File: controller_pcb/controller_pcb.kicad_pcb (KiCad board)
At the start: 2 copper layers, 64.5 x 51.5 mm, 0 parts

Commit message: PCB layout editing
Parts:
- added C1: CL21B106KOQNNNE, Controller_Footprints:CAPC2012X140N, F.Cu at (185.0, 107.5)
- added C2: CL21B106KOQNNNE, Controller_Footprints:CAPC2012X140N, F.Cu at (185.0, 110.3)
- added C3: CL21B106KOQNNNE, Controller_Footprints:CAPC2012X140N, F.Cu at (185.0, 113.1)
- added C4: CL21B106KOQNNNE, Controller_Footprints:CAPC2012X140N, F.Cu at (185.0, 115.9)
- added C5: CL21B106KOQNNNE, Controller_Footprints:CAPC2012X140N, F.Cu at (185.0, 118.7)
- added IC1: ATTINY85V-10SU, Controller_Footprints:SOIC127P798X216-8N, F.Cu at (181.8, 132.1)
- added R1: ERJP06F1002V, Controller_Footprints:ERJP06D1000V, F.Cu at (109.7, 107.0)
- added R2: ERJP06F1002V, Controller_Footprints:ERJP06D1000V, F.Cu at (109.7, 114.0)
- added R3: ERJP06F1002V, Controller_Footprints:ERJP06D1000V, F.Cu at (154.7, 106.5)
- added R4: ERJP06F1002V, Controller_Footprints:ERJP06D1000V, F.Cu at (154.8, 112.0)
- added R5: ERJP06F1002V, Controller_Footprints:ERJP06D1000V, F.Cu at (154.8, 117.0)
- added S1: B3F-1050, Controller_Footprints:B3F1000, F.Cu at (133.2, 108.8)
- added S2: B3F-1050, Controller_Footprints:B3F1000, F.Cu at (151.8, 127.2)
- added S3: B3F-1050, Controller_Footprints:B3F1000, F.Cu at (133.2, 145.8)
- added S4: B3F-1050, Controller_Footprints:B3F1000, F.Cu at (114.8, 127.2)
- added S5: B3F-1050, Controller_Footprints:B3F1000, F.Cu at (133.2, 127.2)
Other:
- board size 64.5 x 51.5 mm -> 64.5 x 53.5 mm
- copper layers 2 -> 4

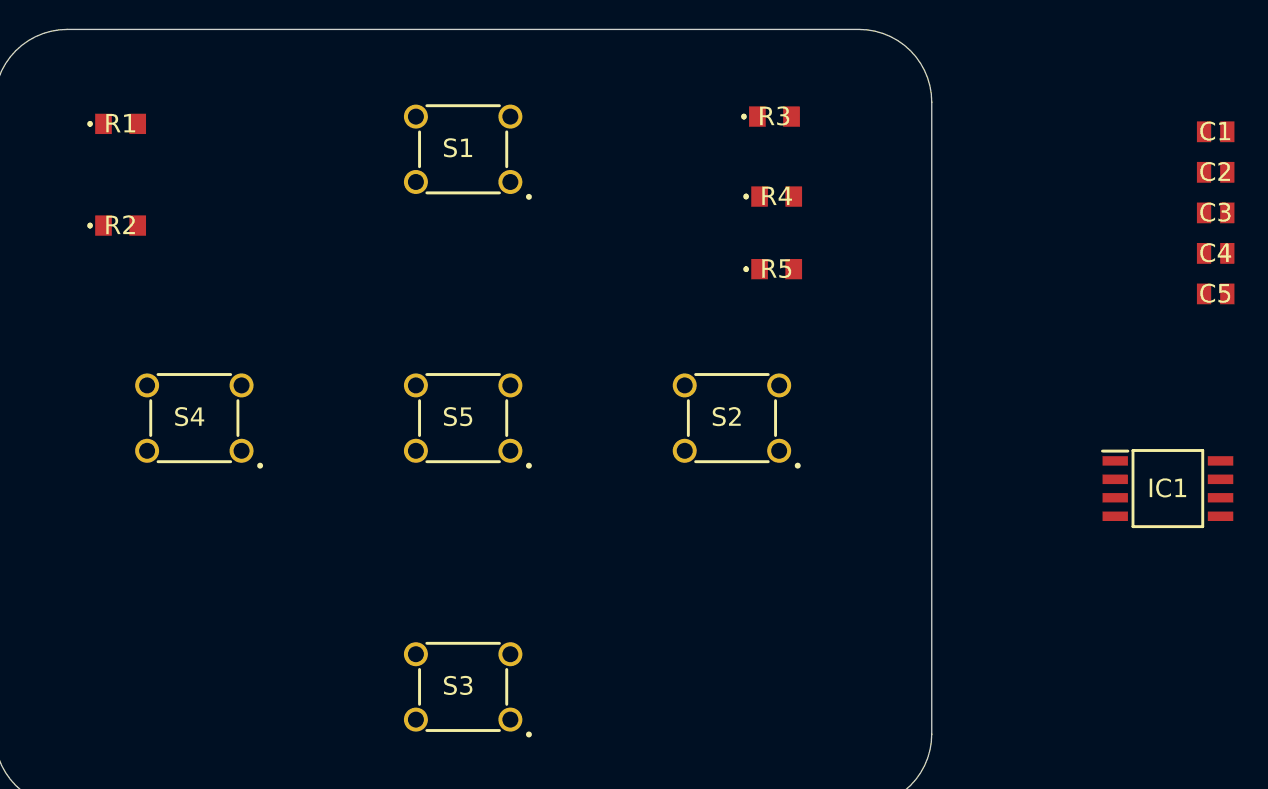
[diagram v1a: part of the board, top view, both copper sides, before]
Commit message: Placed most components, added mounting holes
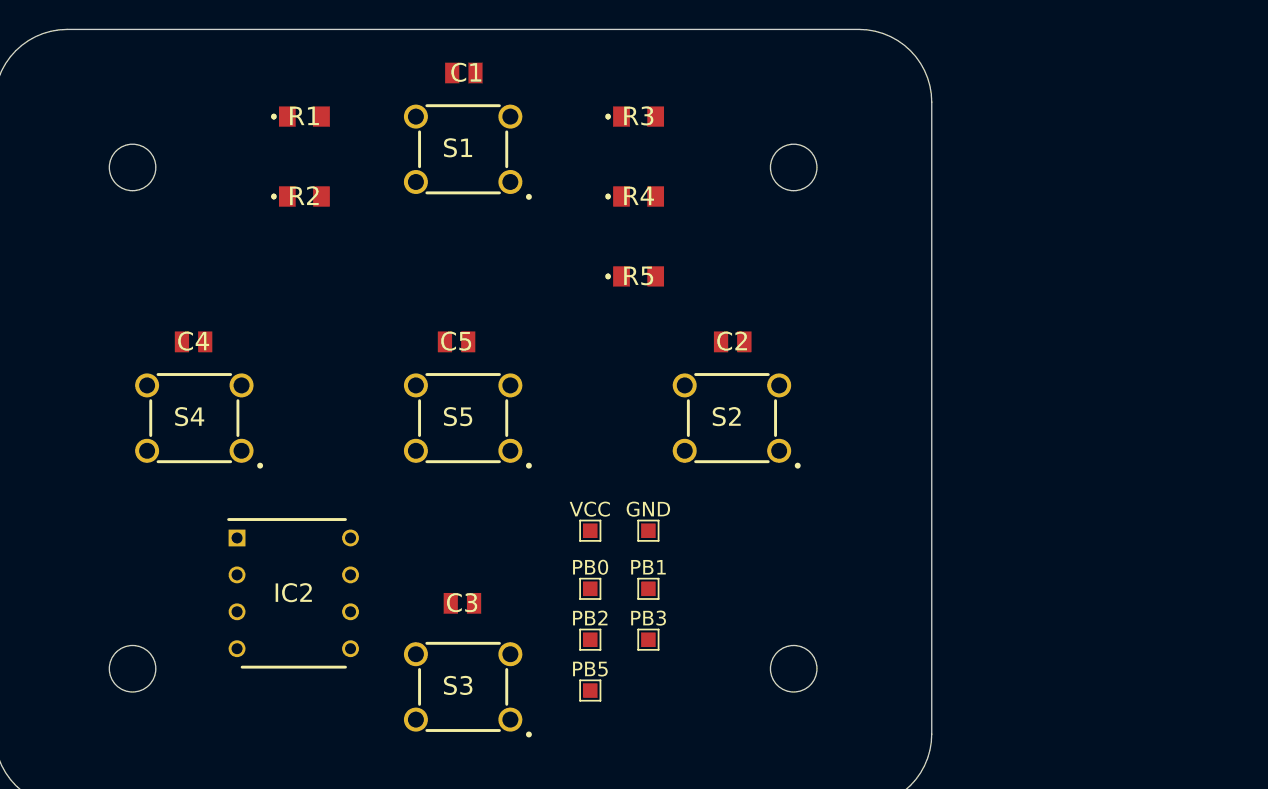
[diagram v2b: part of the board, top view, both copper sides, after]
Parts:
- removed IC1: ATTINY85V-10SU, Controller_Footprints:SOIC127P798X216-8N
- added GND: TestPoint_Pad_1.0x1.0mm, TestPoint:TestPoint_Pad_1.0x1.0mm, F.Cu at (146.0, 135.0)
- added IC2: ATTINY85-20PU, Controller_Footprints:DIP781W56P254L950H533Q8N, F.Cu at (121.6, 139.3)
- added PB0: TestPoint_Pad_1.0x1.0mm, TestPoint:TestPoint_Pad_1.0x1.0mm, F.Cu at (142.0, 139.0)
- added PB1: TestPoint_Pad_1.0x1.0mm, TestPoint:TestPoint_Pad_1.0x1.0mm, F.Cu at (146.0, 139.0)
- added PB2: TestPoint_Pad_1.0x1.0mm, TestPoint:TestPoint_Pad_1.0x1.0mm, F.Cu at (142.0, 142.5)
- added PB3: TestPoint_Pad_1.0x1.0mm, TestPoint:TestPoint_Pad_1.0x1.0mm, F.Cu at (146.0, 142.5)
- added PB5: TestPoint_Pad_1.0x1.0mm, TestPoint:TestPoint_Pad_1.0x1.0mm, F.Cu at (142.0, 146.0)
- added REF**: MountingHole_3.2mm_M3, MountingHole:MountingHole_3.2mm_M3, F.Cu at (110.5, 110.0)
- added REF**: MountingHole_3.2mm_M3, MountingHole:MountingHole_3.2mm_M3, F.Cu at (110.5, 144.5)
- added REF**: MountingHole_3.2mm_M3, MountingHole:MountingHole_3.2mm_M3, F.Cu at (156.0, 144.5)
- added REF**: MountingHole_3.2mm_M3, MountingHole:MountingHole_3.2mm_M3, F.Cu at (156.0, 110.0)
- added VCC: TestPoint_Pad_1.0x1.0mm, TestPoint:TestPoint_Pad_1.0x1.0mm, F.Cu at (142.0, 135.0)
- moved C4 70.6 mm to (114.7, 122.0)
- moved C3 58.4 mm to (133.2, 140.0)
- moved C5 52.3 mm to (132.8, 122.0)
- moved C1 51.9 mm to (133.3, 103.5)
- moved C2 35.2 mm to (151.8, 122.0)
- moved R2 12.8 mm to (122.3, 112.0)
- moved R1 12.7 mm to (122.3, 106.5)
- moved R5 9.51 mm to (145.3, 117.5)
- moved R4 9.50 mm to (145.3, 112.0)
- moved R3 9.35 mm to (145.3, 106.5)

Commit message: Saved unsaved changes
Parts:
- removed GND, PB0, PB1, PB2, PB3, PB5, VCC: TestPoint_Pad_1.0x1.0mm, TestPoint:TestPoint_Pad_1.0x1.0mm

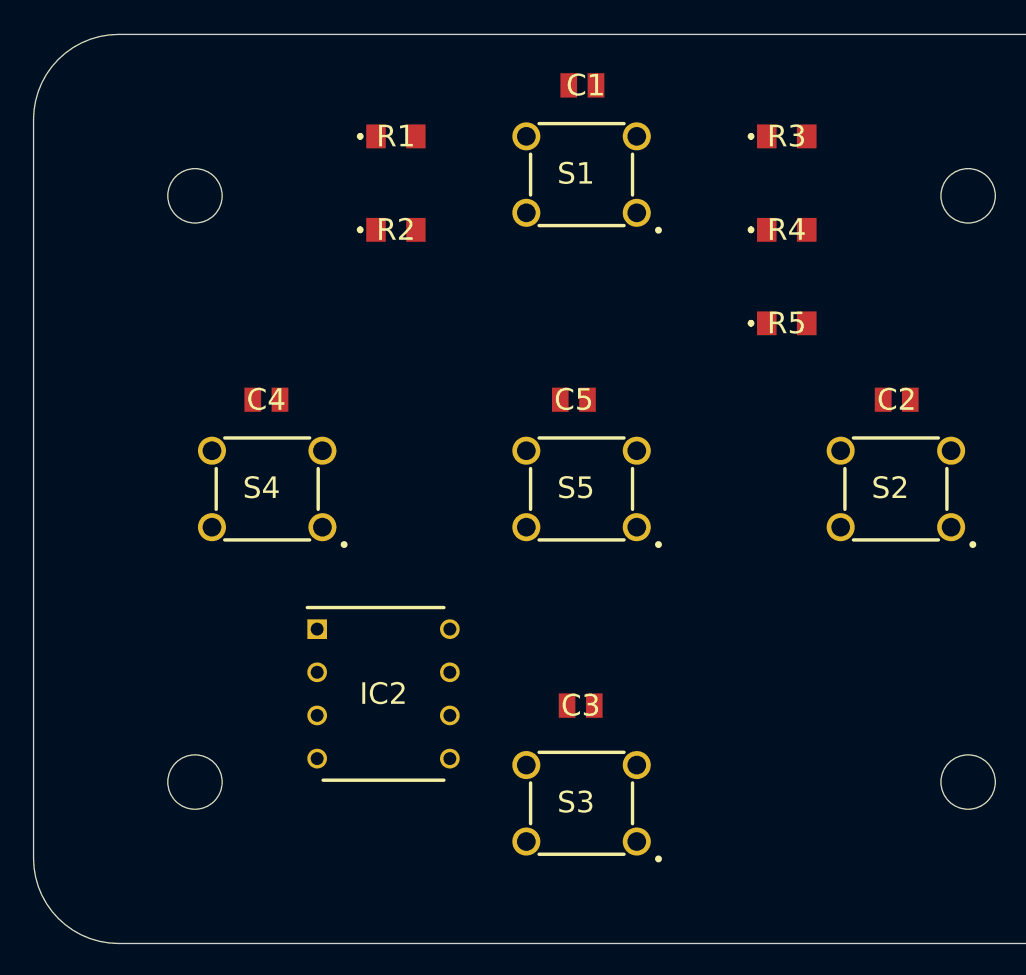
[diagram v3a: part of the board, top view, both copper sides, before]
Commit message: Replaced voltage regulator, added 3D files
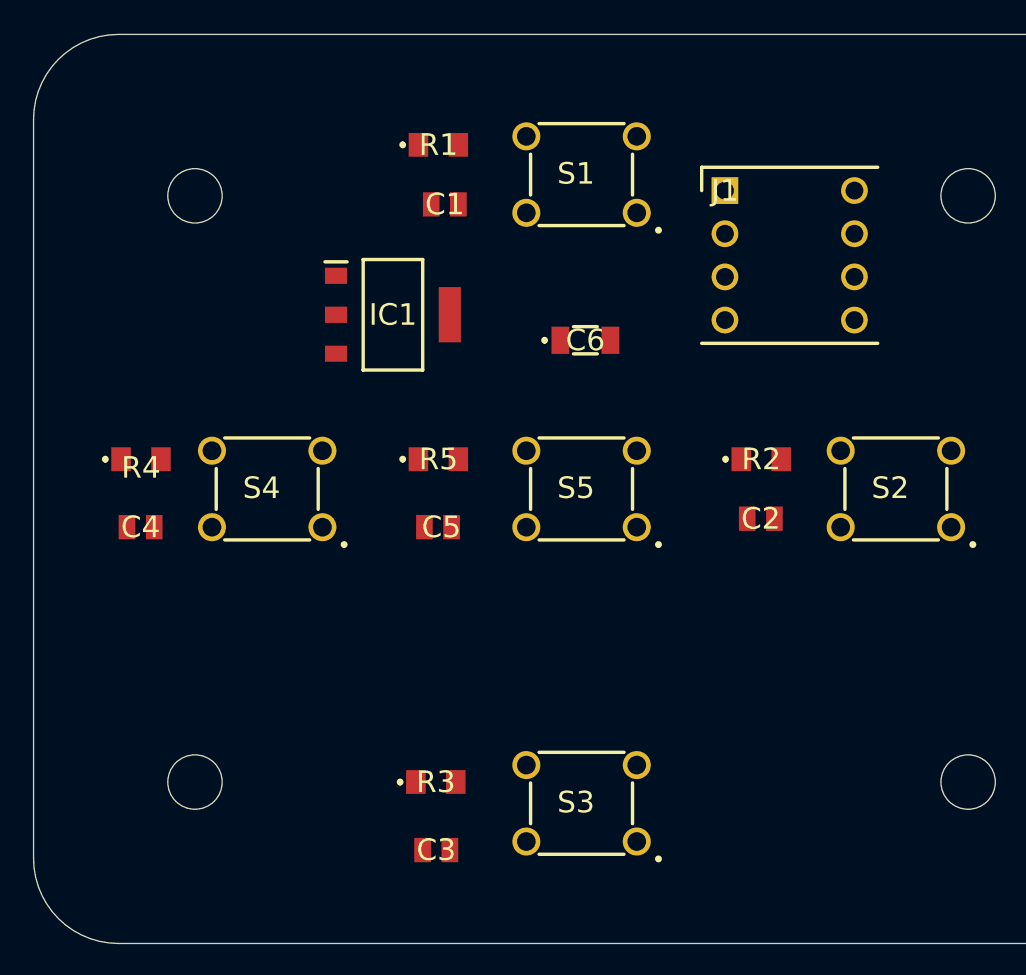
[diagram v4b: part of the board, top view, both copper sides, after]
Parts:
- removed IC2: ATTINY85-20PU, Controller_Footprints:DIP781W56P254L950H533Q8N
- added C6: GRM31CR61A107MEA8L, Controller_Footprints:GRM31x, F.Cu at (133.5, 118.5)
- added IC1: AMS1117-5.0, Controller_Footprints:SOT229P700X180-4N, F.Cu at (122.2, 117.0)
- added J1: A_08-LC-TT, Controller_Footprints:DIPS762W61P254L1016H525Q8N, F.Cu at (141.7, 109.7)
- moved R3 43.2 mm to (124.7, 144.5)
- moved R4 40.3 mm to (107.3, 125.5)
- moved R2 25.4 mm to (143.8, 125.5)
- moved R5 22.0 mm to (124.8, 125.5)
- moved C3 12.0 mm to (124.7, 148.5)
- moved C5 11.0 mm to (124.8, 129.5)
- moved C1 10.7 mm to (125.2, 110.5)
- moved C2 10.6 mm to (143.8, 129.0)
- moved C4 10.5 mm to (107.3, 129.5)
- moved R1 2.55 mm to (124.8, 107.0)
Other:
- copper layers 4 -> 2

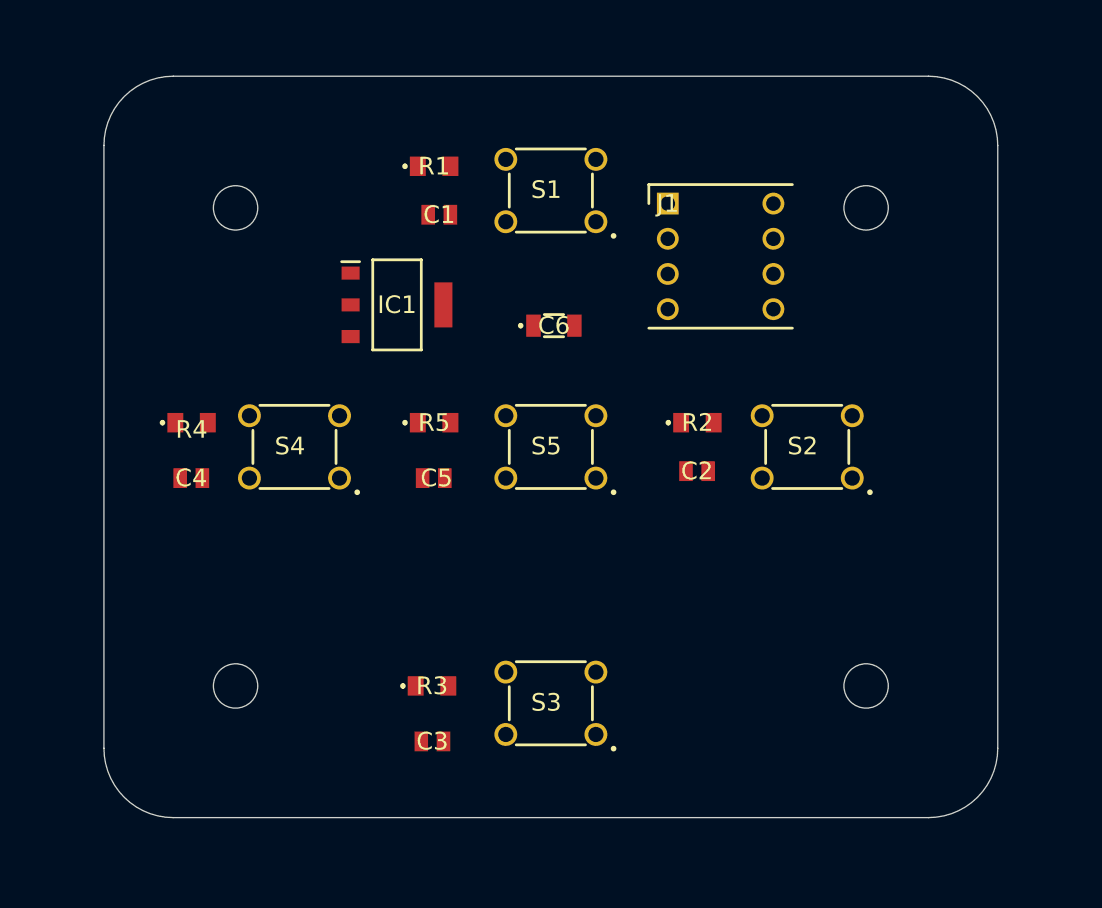
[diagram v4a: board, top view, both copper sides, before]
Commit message: MOSFET, regulator, PWR_LED, JST added; half routed; ground plane created
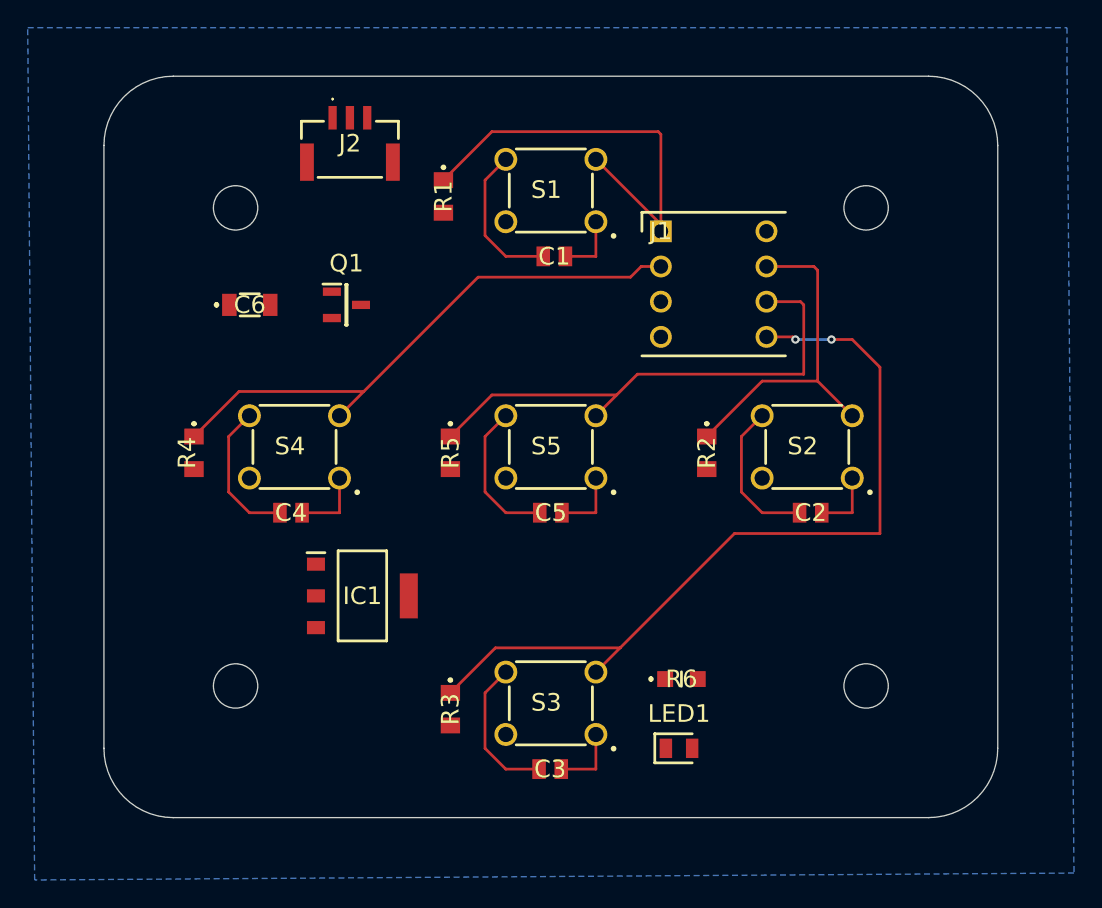
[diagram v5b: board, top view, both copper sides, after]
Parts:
- added J2: SM03B-GHS-TB_LF__SN_, Controller_Footprints:SM03BGHSTBLFSN, F.Cu at (118.8, 105.3)
- added LED1: 150080RS75000, Controller_Footprints:LEDC2012X70N, F.Cu at (142.5, 149.0)
- added Q1: SI2301CDS-T1-GE3., Controller_Footprints:SOT95P237X112-3N, F.Cu at (118.5, 117.0)
- added R6: ERJ-6ENF2200V, Controller_Footprints:ERJ6ENF1000V, F.Cu at (142.7, 144.0)
- moved C6 22.0 mm to (111.5, 117.0)
- moved IC1 21.1 mm to (119.7, 138.0)
- moved C1 8.83 mm to (133.5, 113.5), turned to 180 degrees
- moved C5 8.81 mm to (133.2, 132.0), turned to 180 degrees
- moved C3 8.73 mm to (133.2, 150.5), turned to 180 degrees
- moved C2 8.73 mm to (152.0, 132.0), turned to 180 degrees
- moved C4 7.62 mm to (114.5, 132.0), turned to 180 degrees
- moved R5 2.47 mm to (126.0, 127.7), turned to -90 degrees
- moved R2 2.28 mm to (144.5, 127.7), turned to -90 degrees
- moved R1 2.28 mm to (125.5, 109.2), turned to -90 degrees
- moved R4 2.18 mm to (107.5, 127.7), turned to -90 degrees
- moved R3 2.14 mm to (126.0, 146.2), turned to -90 degrees
- moved J1 2.06 mm to (141.2, 111.7)
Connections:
- J1 pad 5: Net-(J1-Pad5) -> Net-(IC1-VOUT)
- J1 pad 8: Net-(IC1-VIN) -> Net-(IC1-VOUT)
- R1 pad 1: Net-(J1-Pad5) -> Net-(J1-Pad1)
- R2 pad 1: Net-(J1-Pad6) -> Net-(J1-Pad7)
- R3 pad 1: Net-(J1-Pad7) -> Net-(IC1-VOUT)
- R4 pad 1: Net-(IC1-VOUT) -> Net-(J1-Pad2)
- R4 pad 2: Net-(J1-Pad2) -> Net-(IC1-VOUT)
- R5 pad 2: Net-(J1-Pad1) -> Net-(J1-Pad6)
- S2 pad 3: Net-(J1-Pad2) -> Net-(IC1-VOUT)
- S3 pad 1: GND -> Net-(C3-Pad1)
- S3 pad 2: Net-(C3-Pad2) -> GND
- S3 pad 3: Net-(C3-Pad1) -> Net-(IC1-VOUT)
- S3 pad 4: Net-(J1-Pad5) -> Net-(C3-Pad2)
- S4 pad 1: GND -> Net-(C4-Pad1)
- S4 pad 2: Net-(C4-Pad2) -> GND
- S4 pad 3: Net-(C4-Pad1) -> Net-(J1-Pad2)
- S4 pad 4: Net-(J1-Pad6) -> Net-(C4-Pad2)
- S5 pad 1: GND -> Net-(C5-Pad1)
- S5 pad 2: Net-(C5-Pad2) -> GND
- S5 pad 3: Net-(C5-Pad1) -> Net-(IC1-VOUT)
- S5 pad 4: Net-(J1-Pad7) -> Net-(C5-Pad2)
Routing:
- net Net-(IC1-VOUT): track 0.00 -> 96.6 mm, vias 0 -> 2
- net Net-(J1-Pad2): track 0.00 -> 41.2 mm
- net Net-(J1-Pad1): track 0.00 -> 31.4 mm
- net Net-(J1-Pad7): track 0.00 -> 25.0 mm
- net Net-(C2-Pad2): track 0.00 -> 10.9 mm
- net Net-(C1-Pad2): track 0.00 -> 10.9 mm
- net Net-(C5-Pad2): track 0.00 -> 10.7 mm
- net Net-(C3-Pad2): track 0.00 -> 10.6 mm
- net Net-(C4-Pad2): track 0.00 -> 10.4 mm
- net Net-(C4-Pad1): track 0.00 -> 5.20 mm
- net Net-(C3-Pad1): track 0.00 -> 5.00 mm
- net Net-(C1-Pad1): track 0.00 -> 5.00 mm
- net Net-(C5-Pad1): track 0.00 -> 4.95 mm
- net Net-(C2-Pad1): track 0.00 -> 4.70 mm
- added copper zone on B.Cu, net GND

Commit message: 3D models added
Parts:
- moved C6 1.08 mm to (112.5, 117.5), turned to 90 degrees
- moved Q1 1.07 mm to (119.5, 117.5)
- turned J2 to 180 degrees
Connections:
- J2 pad 1: unconnected-(J2-Pad1) -> GND
- LED1 pad 1: unconnected-(LED1-K-Pad1) -> GND
- LED1 pad 2: unconnected-(LED1-A-Pad2) -> Net-(LED1-A)
- R6 pad 1: unconnected-(R6-Pad1) -> Net-(LED1-A)
- R6 pad 2: unconnected-(R6-Pad2) -> Net-(IC1-VOUT)
